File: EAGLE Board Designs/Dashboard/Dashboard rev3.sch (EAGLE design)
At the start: 84 parts, among them J2 CONNECTOR-8_NF_S_RA_BLACK, J3 CONNECTOR-CAN_NF_S_RA_BLACK, J4 CONNECTOR-AVR-ISP_2X05_SMD_, K1 CPC1002N, Q1 TRANSISTOR_N_MOS__PMV15ENEA, Q2 TRANSISTOR_N_MOS__PMV15ENEA, Q3 TRANSISTOR_N_MOS__PMV15ENEA, Q4 TRANSISTOR_N_MOS__PMV15ENEA, Q5 TRANSISTOR_N_MOS__PMV15ENEA, Q6 TRANSISTOR_N_MOS__PMV15ENEA, U1 ATMEGA328P-AU, U2 TCAN1051HQV-Q1, U3 MCP2515, U4 MCP23S17, U5 CONVERTER_DC/DC_12V-5V, X1 CRYSTAL16MHZ, X2 CRYSTAL16MHZ, X7 CONNECTOR-8NANO-FIT_RIGHT_ANG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

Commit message: Minor changes
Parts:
- added R16: RESISTOR_0603_154K, HyTechDevices:RESISTOR_0603_154K
- added R19: RESISTOR_0603_4.12K, HyTechDevices:RESISTOR_0603_4.12K
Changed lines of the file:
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@@
 <part name="P1" library="HyTechSupplies" deviceset="GND" device=""/>
 <part name="U$1" library="HyTechDevices" deviceset="BUZZER_3_PIN_" device="" technology="CPT-3011C-120"/>
+<part name="R16" library="HyTechDevices" deviceset="RESISTOR_?_*" device="0603" technology="154K"/>
+<part name="R19" library="HyTechDevices" deviceset="RESISTOR_?_*" device="0603" technology="4.12K"/>
 </parts>
 <sheets>
@@
 <attribute name="MPN" x="116.84" y="40.64" size="1.27" layer="96" align="top-left"/>
 </instance>
+<instance part="R16" gate="G$1" x="88.9" y="35.56" smashed="yes" rot="R90">
+<attribute name="NAME" x="87.63" y="34.29" size="1.27" layer="95" rot="R90" align="bottom-center"/>
+<attribute name="RESISTANCE" x="90.17" y="34.29" size="1.27" layer="96" rot="R90" align="top-center"/>
+</instance>
+<instance part="R19" gate="G$1" x="99.06" y="38.1" smashed="yes" rot="R180">
+<attribute name="NAME" x="100.33" y="36.83" size="1.27" layer="95" rot="R180" align="bottom-center"/>
+<attribute name="RESISTANCE" x="100.33" y="39.37" size="1.27" layer="96" rot="R180" align="top-center"/>
+</instance>
 </instances>

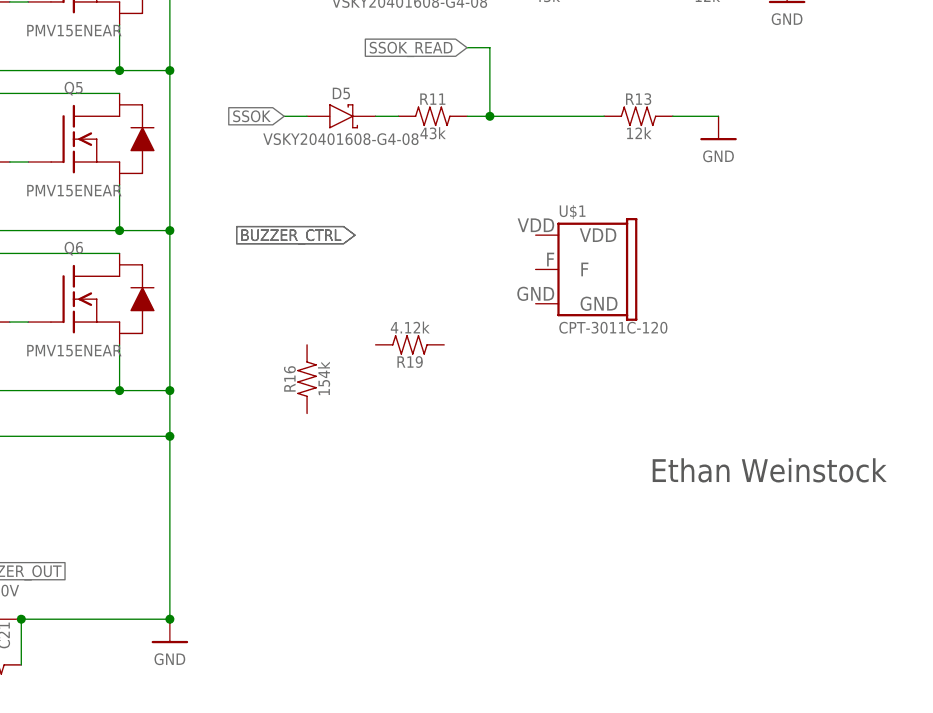
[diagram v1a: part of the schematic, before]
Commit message: Added buzzer circuit
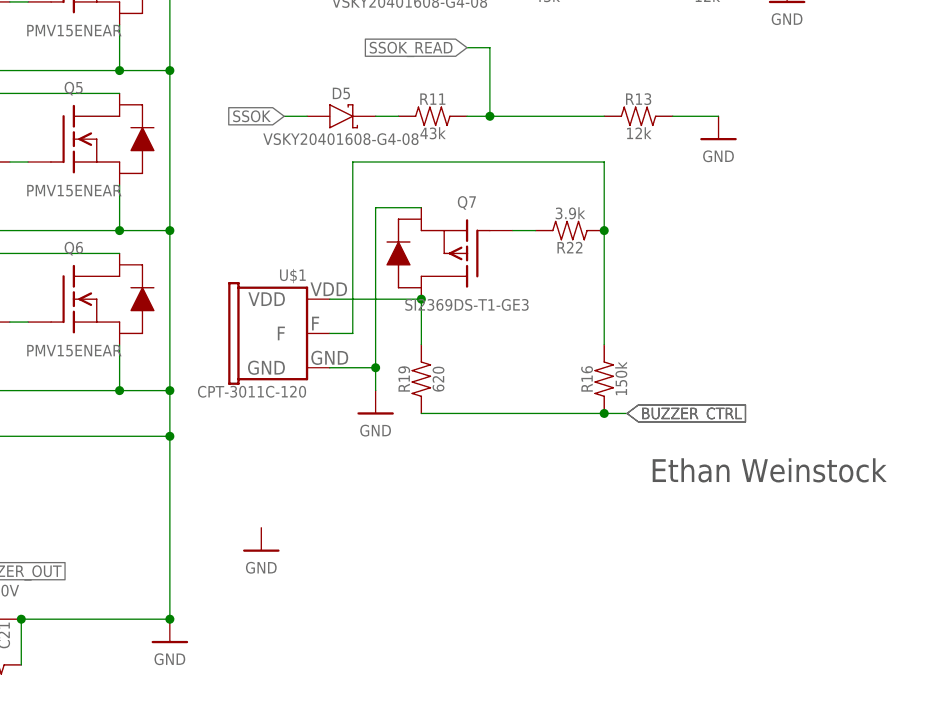
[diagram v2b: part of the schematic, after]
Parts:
- added Q7: TRANSISTOR_P_MOS_SOT23_SI2369DS-T1-GE3, HyTechDevices:TRANSISTOR_P_MOS_SOT23_SI2369DS-T1-GE3
- added R22: RESISTOR_0603_3.9K, HyTechDevices:RESISTOR_0603_3.9K
- R16: value RESISTOR_0603_154K -> RESISTOR_0603_150K; device HyTechDevices:RESISTOR_0603_154K -> HyTechDevices:RESISTOR_0603_150K
- R19: value RESISTOR_0603_4.12K -> RESISTOR_0603_620; device HyTechDevices:RESISTOR_0603_4.12K -> HyTechDevices:RESISTOR_0603_620
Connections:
- new net N$20: R16.2, R22.1, U$1.F
- new net N$22: Q7.G, R22.2
- new net N$29: R16.1, R19.1
- new net N$41: Q7.D, R19.2, U$1.VDD
- net GND: now also Q7.S, U$1.GND
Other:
- moved on the sheet: R16, R19, U$1
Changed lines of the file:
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@@
 <part name="P1" library="HyTechSupplies" deviceset="GND" device=""/>
 <part name="U$1" library="HyTechDevices" deviceset="BUZZER_3_PIN_" device="" technology="CPT-3011C-120"/>
-<part name="R16" library="HyTechDevices" deviceset="RESISTOR_?_*" device="0603" technology="154K"/>
-<part name="R19" library="HyTechDevices" deviceset="RESISTOR_?_*" device="0603" technology="4.12K"/>
+<part name="R16" library="HyTechDevices" deviceset="RESISTOR_?_*" device="0603" technology="150K"/>
+<part name="R19" library="HyTechDevices" deviceset="RESISTOR_?_*" device="0603" technology="620"/>
+<part name="P14" library="HyTechSupplies" deviceset="GND" device=""/>
+<part name="R22" library="HyTechDevices" deviceset="RESISTOR_?_*" device="0603" technology="3.9K"/>
+<part name="Q7" library="HyTechDevices" deviceset="TRANSISTOR_P_MOS_?_*" device="SOT23" technology="SI2369DS-T1-GE3"/>
+<part name="P24" library="HyTechSupplies" deviceset="GND" device=""/>
 </parts>
 <sheets>
@@
 <attribute name="VALUE" x="198.12" y="123.19" size="1.27" layer="96" align="top-center"/>
 </instance>
-<instance part="U$1" gate="G$1" x="116.84" y="51.562" smashed="yes">
-<attribute name="NAME" x="116.84" y="52.324" size="1.27" layer="95"/>
-<attribute name="MPN" x="116.84" y="40.64" size="1.27" layer="96" align="top-left"/>
-</instance>
-<instance part="R16" gate="G$1" x="88.9" y="35.56" smashed="yes" rot="R90">
-<attribute name="NAME" x="87.63" y="34.29" size="1.27" layer="95" rot="R90" align="bottom-center"/>
-<attribute name="RESISTANCE" x="90.17" y="34.29" size="1.27" layer="96" rot="R90" align="top-center"/>
-</instance>
-<instance part="R19" gate="G$1" x="99.06" y="38.1" smashed="yes" rot="R180">
-<attribute name="NAME" x="100.33" y="36.83" size="1.27" layer="95" rot="R180" align="bottom-center"/>
-<attribute name="RESISTANCE" x="100.33" y="39.37" size="1.27" layer="96" rot="R180" align="top-center"/>
+<instance part="U$1" gate="G$1" x="88.9" y="44.45" smashed="yes" rot="MR0">
+<attribute name="NAME" x="88.9" y="45.212" size="1.27" layer="95" rot="MR0"/>
+<attribute name="MPN" x="88.9" y="33.528" size="1.27" layer="96" rot="MR0" align="top-left"/>
+</instance>
+<instance part="R16" gate="G$1" x="121.92" y="35.56" smashed="yes" rot="R90">
+<attribute name="NAME" x="120.65" y="34.29" size="1.27" layer="95" rot="R90" align="bottom-center"/>
+<attribute name="RESISTANCE" x="123.19" y="34.29" size="1.27" layer="96" rot="R90" align="top-center"/>
+</instance>
+<instance part="R19" gate="G$1" x="101.6" y="35.56" smashed="yes" rot="R90">
+<attribute name="NAME" x="100.33" y="34.29" size="1.27" layer="95" rot="R90" align="bottom-center"/>
+<attribute name="RESISTANCE" x="102.87" y="34.29" size="1.27" layer="96" rot="R90" align="top-center"/>
+</instance>
+<instance part="P14" gate="1" x="83.82" y="15.24" smashed="yes">
+<attribute name="VALUE" x="83.82" y="13.97" size="1.27" layer="96" align="top-center"/>
+</instance>
+<instance part="R22" gate="G$1" x="116.84" y="50.8" smashed="yes" rot="R180">
+<attribute name="NAME" x="118.11" y="49.53" size="1.27" layer="95" rot="R180" align="bottom-center"/>
+<attribute name="RESISTANCE" x="118.11" y="52.07" size="1.27" layer="96" rot="R180" align="top-center"/>
+</instance>
+<instance part="Q7" gate="G$1" x="106.68" y="48.26" smashed="yes" rot="MR0">
+<attribute name="NAME" x="106.68" y="53.34" size="1.27" layer="95" rot="MR0" align="bottom-center"/>
+<attribute name="MPN" x="106.68" y="43.18" size="1.27" layer="95" rot="MR0" align="top-center"/>
+</instance>
+<instance part="P24" gate="1" x="96.52" y="30.48" smashed="yes">
+<attribute name="VALUE" x="96.52" y="29.21" size="1.27" layer="96" align="top-center"/>
 </instance>
 </instances>
@@
 <junction x="198.12" y="127"/>
 </segment>
+<segment>
+<pinref part="Q7" gate="G$1" pin="S"/>
+<wire x1="101.6" y1="53.34" x2="96.52" y2="53.34" width="0.1524" layer="91"/>
+<pinref part="U$1" gate="G$1" pin="GND"/>
+<wire x1="96.52" y1="53.34" x2="96.52" y2="35.56" width="0.1524" layer="91"/>
+<wire x1="96.52" y1="35.56" x2="91.44" y2="35.56" width="0.1524" layer="91"/>
+<pinref part="P24" gate="1" pin="GND"/>
+<wire x1="96.52" y1="33.02" x2="96.52" y2="35.56" width="0.1524" layer="91"/>
+<junction x="96.52" y="35.56"/>
+</segment>
 </net>
 <net name="+5V" class="0">
@@
 <pinref part="K1" gate="G$1" pin="CONTROL+"/>
 <wire x1="26.67" y1="12.7" x2="24.13" y2="12.7" width="0.1524" layer="91"/>
-<label x="94.234" y="50.292" size="1.27" layer="95" rot="R180" xref="yes"/>
-<label x="94.234" y="50.292" size="1.27" layer="95" rot="R180" xref="yes"/>
+<label x="124.46" y="30.48" size="1.27" layer="95" xref="yes"/>
+<label x="124.46" y="30.48" size="1.27" layer="95" xref="yes"/>
 </segment>
 </net>
@@
 </segment>
 </net>
+<net name="N$20" class="0">
+<segment>
+<pinref part="R16" gate="G$1" pin="2"/>
+<pinref part="R22" gate="G$1" pin="1"/>
+<wire x1="121.92" y1="38.1" x2="121.92" y2="50.8" width="0.1524" layer="91"/>
+<pinref part="U$1" gate="G$1" pin="F"/>
+<wire x1="91.44" y1="39.37" x2="93.98" y2="39.37" width="0.1524" layer="91"/>
+<wire x1="93.98" y1="39.37" x2="93.98" y2="58.42" width="0.1524" layer="91"/>
+<wire x1="93.98" y1="58.42" x2="121.92" y2="58.42" width="0.1524" layer="91"/>
+<wire x1="121.92" y1="58.42" x2="121.92" y2="50.8" width="0.1524" layer="91"/>
+<junction x="121.92" y="50.8"/>
+</segment>
+</net>
+<net name="N$29" class="0">
+<segment>
+<wire x1="101.6" y1="30.48" x2="121.92" y2="30.48" width="0.1524" layer="91"/>
+<pinref part="R19" gate="G$1" pin="1"/>
+<pinref part="R16" gate="G$1" pin="1"/>
+<wire x1="121.92" y1="30.48" x2="124.46" y2="30.48" width="0.1524" layer="91"/>
+<junction x="121.92" y="30.48"/>
+</segment>
+</net>
+<net name="N$22" class="0">
+<segment>
+<pinref part="R22" gate="G$1" pin="2"/>
+<pinref part="Q7" gate="G$1" pin="G"/>
+<wire x1="114.3" y1="50.8" x2="111.76" y2="50.8" width="0.1524" layer="91"/>
+</segment>
+</net>
+<net name="N$41" class="0">
+<segment>
+<pinref part="U$1" gate="G$1" pin="VDD"/>
+<pinref part="Q7" gate="G$1" pin="D"/>
+<pinref part="R19" gate="G$1" pin="2"/>
+<wire x1="101.6" y1="38.1" x2="101.6" y2="43.18" width="0.1524" layer="91"/>
+<junction x="101.6" y="43.18"/>
+<wire x1="101.6" y1="43.18" x2="91.44" y2="43.18" width="0.1524" layer="91"/>
+</segment>
+</net>

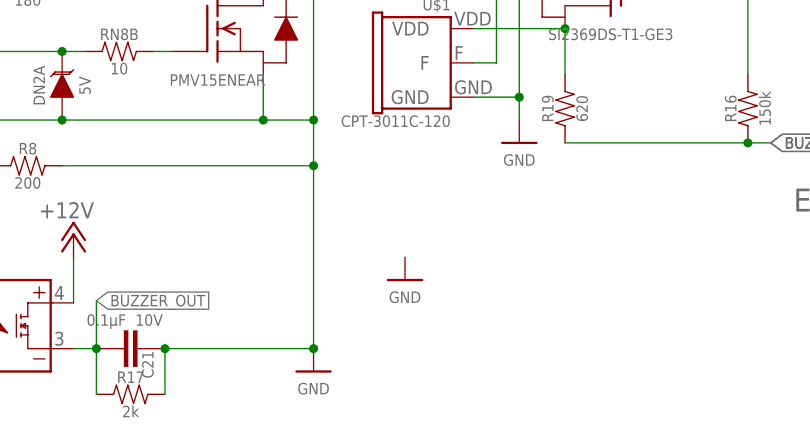
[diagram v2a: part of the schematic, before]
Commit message: Removed extra ground
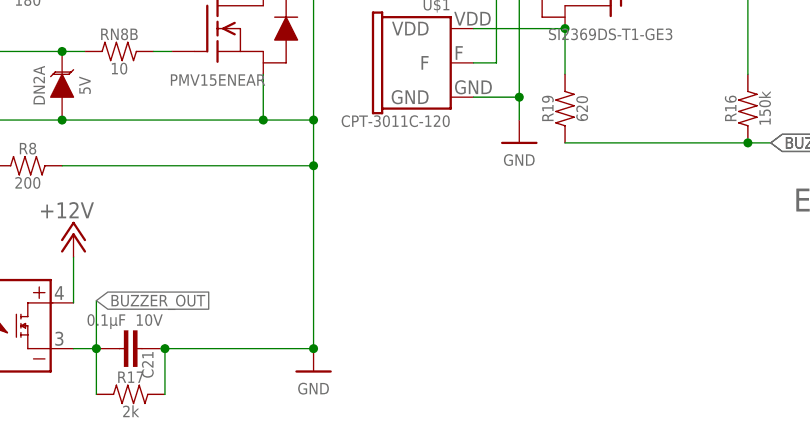
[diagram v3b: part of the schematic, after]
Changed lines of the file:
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@@
 <part name="R16" library="HyTechDevices" deviceset="RESISTOR_?_*" device="0603" technology="150K"/>
 <part name="R19" library="HyTechDevices" deviceset="RESISTOR_?_*" device="0603" technology="620"/>
-<part name="P14" library="HyTechSupplies" deviceset="GND" device=""/>
 <part name="R22" library="HyTechDevices" deviceset="RESISTOR_?_*" device="0603" technology="3.9K"/>
 <part name="Q7" library="HyTechDevices" deviceset="TRANSISTOR_P_MOS_?_*" device="SOT23" technology="SI2369DS-T1-GE3"/>
@@
 <attribute name="RESISTANCE" x="102.87" y="34.29" size="1.27" layer="96" rot="R90" align="top-center"/>
 </instance>
-<instance part="P14" gate="1" x="83.82" y="15.24" smashed="yes">
-<attribute name="VALUE" x="83.82" y="13.97" size="1.27" layer="96" align="top-center"/>
-</instance>
 <instance part="R22" gate="G$1" x="116.84" y="50.8" smashed="yes" rot="R180">

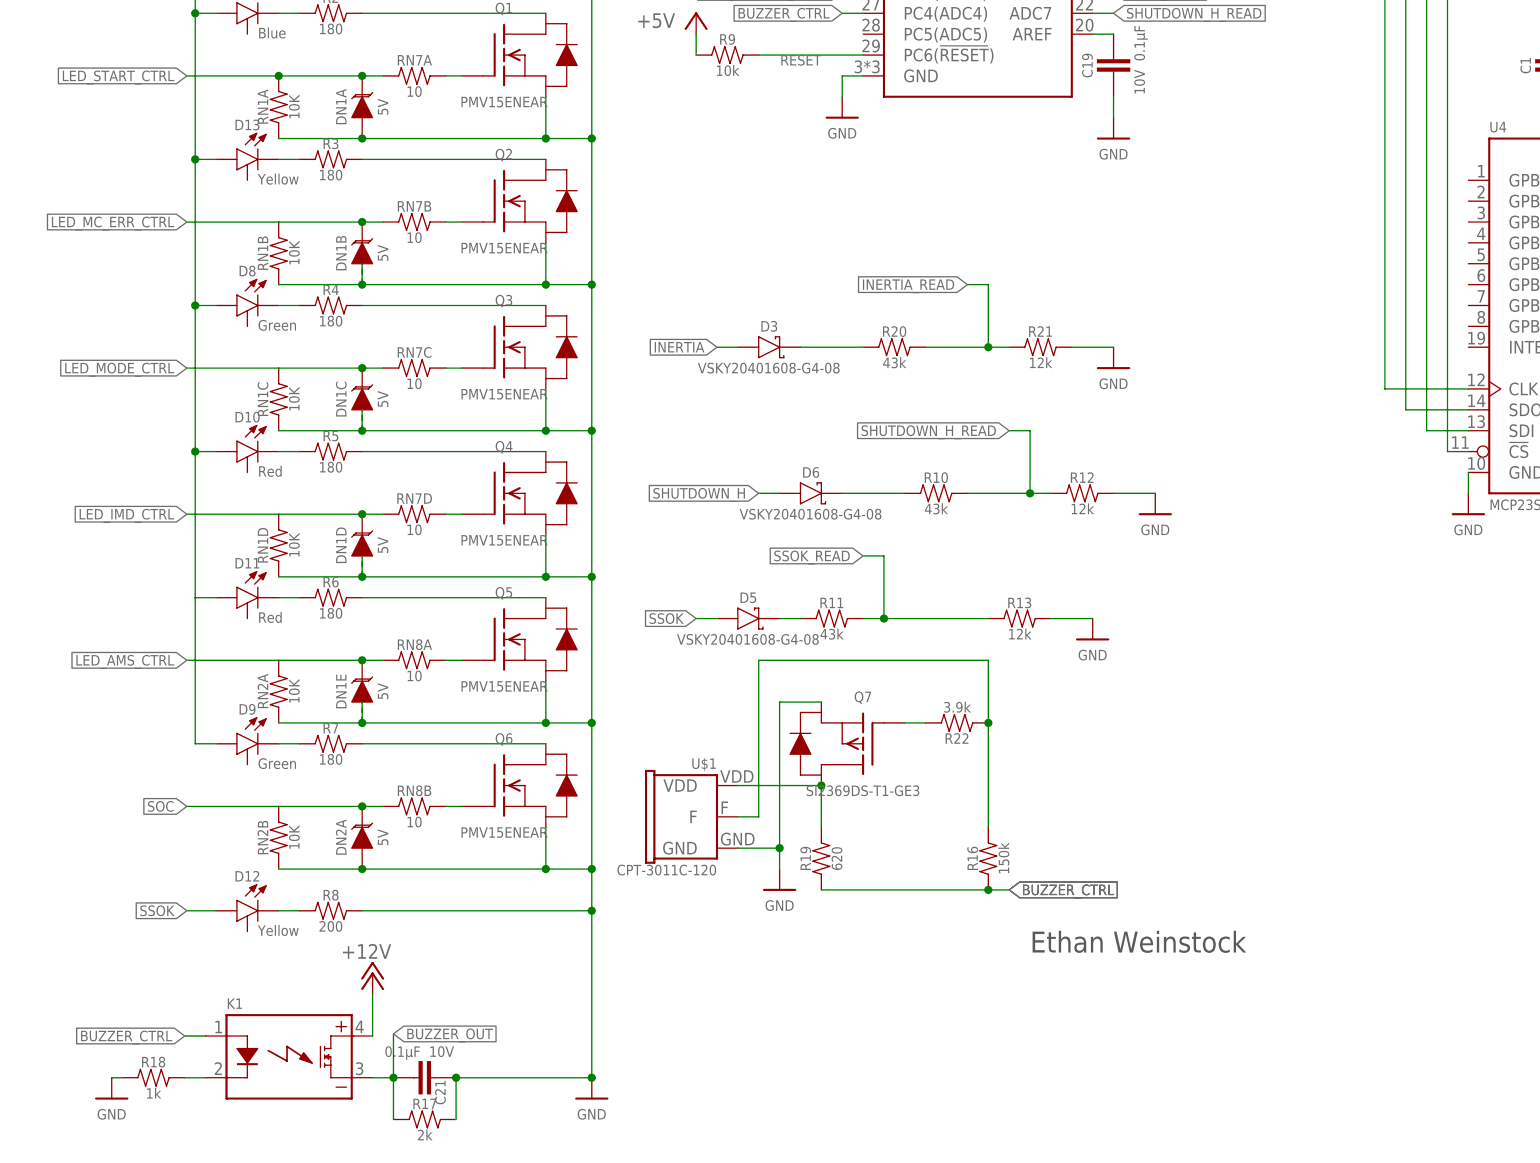
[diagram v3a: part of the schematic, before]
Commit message: Added buzzer out circuit
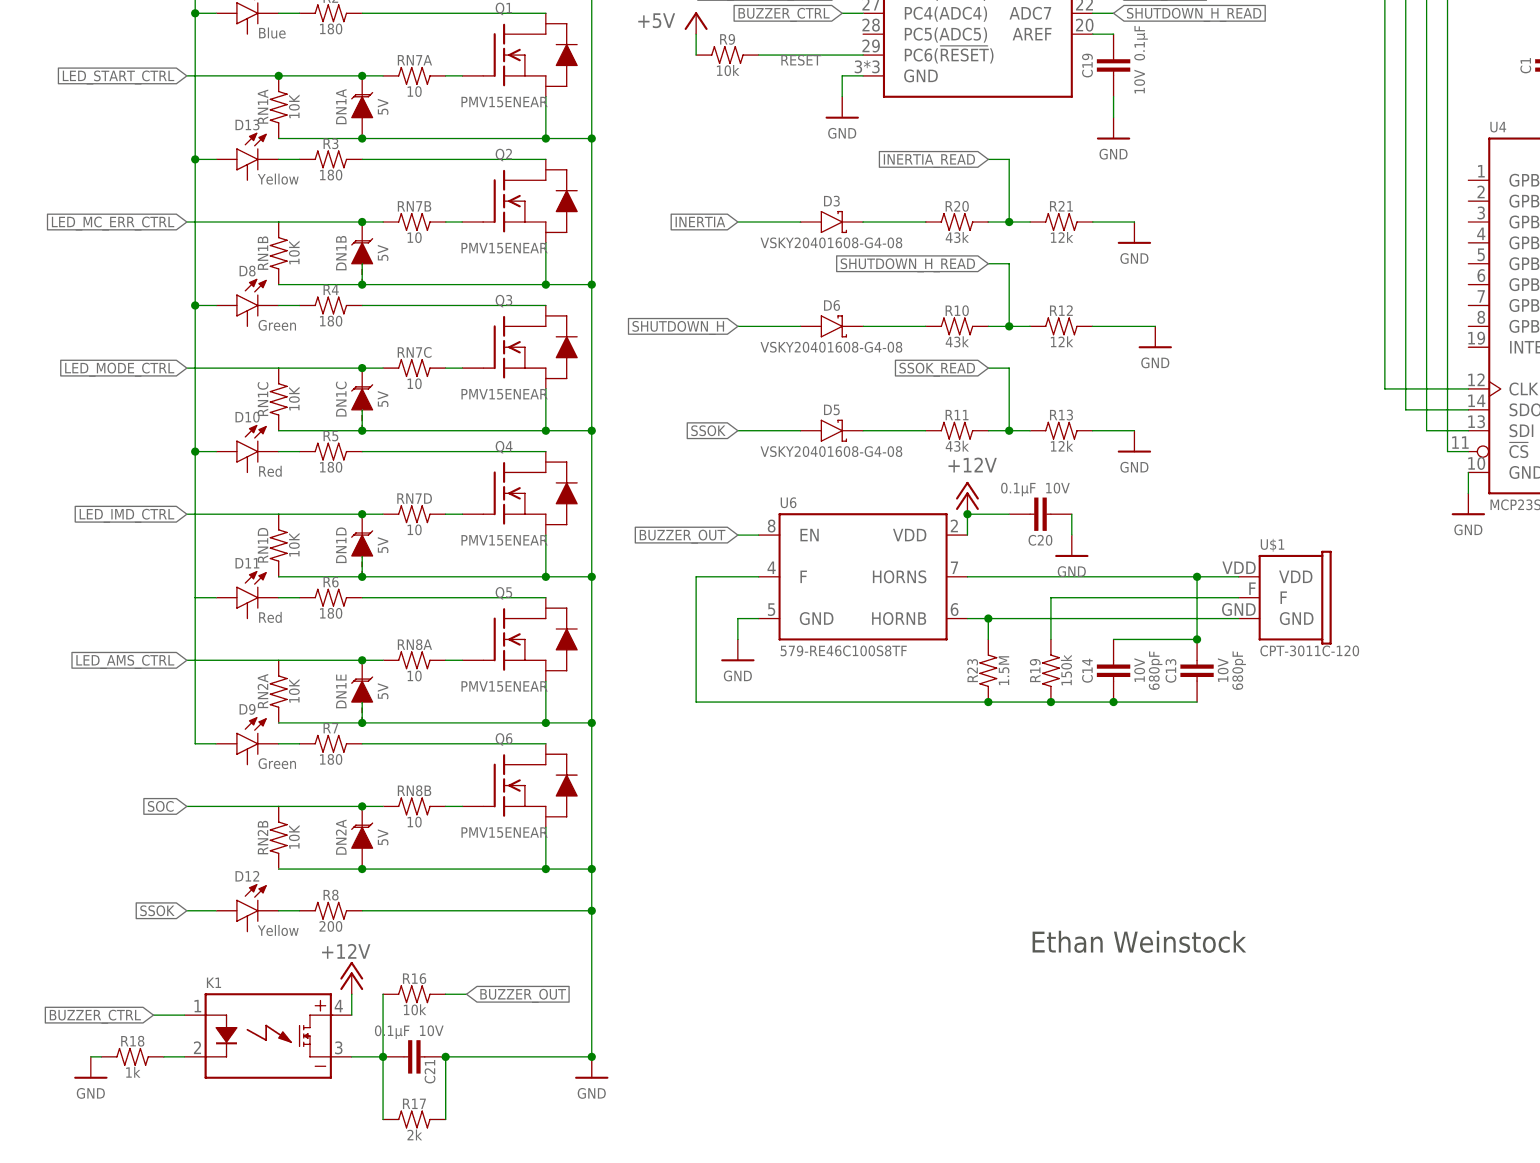
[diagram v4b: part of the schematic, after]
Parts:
- removed Q7: TRANSISTOR_P_MOS_SOT23_SI2369DS-T1-GE3, HyTechDevices:TRANSISTOR_P_MOS_SOT23_SI2369DS-T1-GE3
- removed R22: RESISTOR_0603_3.9K, HyTechDevices:RESISTOR_0603_3.9K
- added C13, C14: CAPACITOR_0603_10V_680PF, HyTechDevices:CAPACITOR_0603_10V_680PF
- added C20: CAPACITOR_0603_10V_0.1UF, HyTechDevices:CAPACITOR_0603_10V_0.1UF
- added R23: RESISTOR_0603_1.5M, HyTechDevices:RESISTOR_0603_1.5M
- added U6: RE46C100, HyTechDevicesTemp:RE46C100
- R16: value RESISTOR_0603_150K -> RESISTOR_0603_10K; device HyTechDevices:RESISTOR_0603_150K -> HyTechDevices:RESISTOR_0603_10K
- R19: value RESISTOR_0603_620 -> RESISTOR_0603_150K; device HyTechDevices:RESISTOR_0603_620 -> HyTechDevices:RESISTOR_0603_150K
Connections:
- new net N$28: R19.2, U$1.F
- new net N$30: C13.1, C14.1, U$1.VDD, U6.HORNS
- net +12V: now also C20.1, U6.VDD
- net BUZZER_OUT: now also R16.1
- net GND: now also C20.2, U6.GND; no longer Q7.S, U$1.GND
- net N$20: now also C13.2, C14.2, R19.1, R23.1, U6.F; no longer R16.2, R22.1, U$1.F
- net N$22: now also U6.EN; no longer Q7.G, R22.2
- net N$29: now also R23.2, U$1.GND, U6.HORNB; no longer R16.1, R19.1
- net N$41: now also R16.2; no longer Q7.D, R19.2, U$1.VDD
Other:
- moved on the sheet: C21, D3, D5, D6, K1, R10, R11, R12, R13, R16, R17, R18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
